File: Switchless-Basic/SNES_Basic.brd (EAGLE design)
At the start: 44.1 x 33 mm, 40 parts

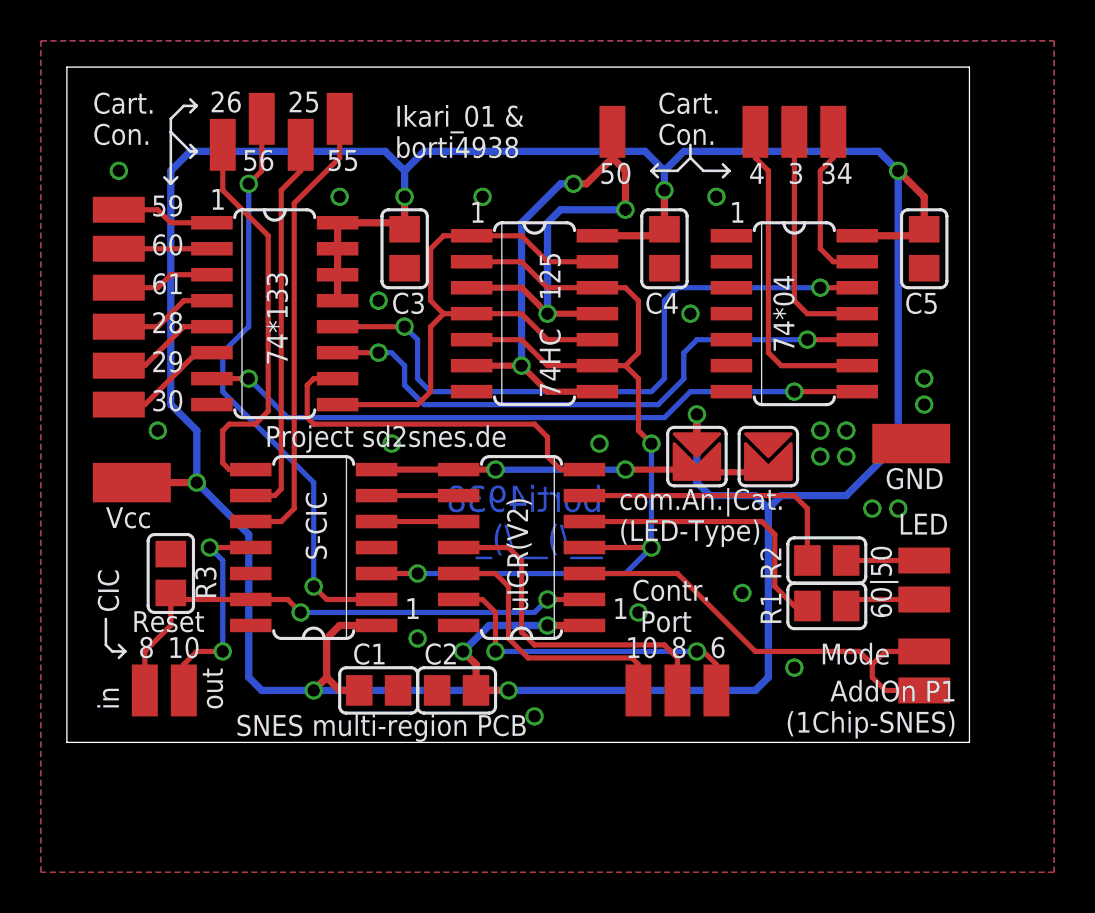
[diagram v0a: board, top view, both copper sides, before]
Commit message: correct two silkscreen errors
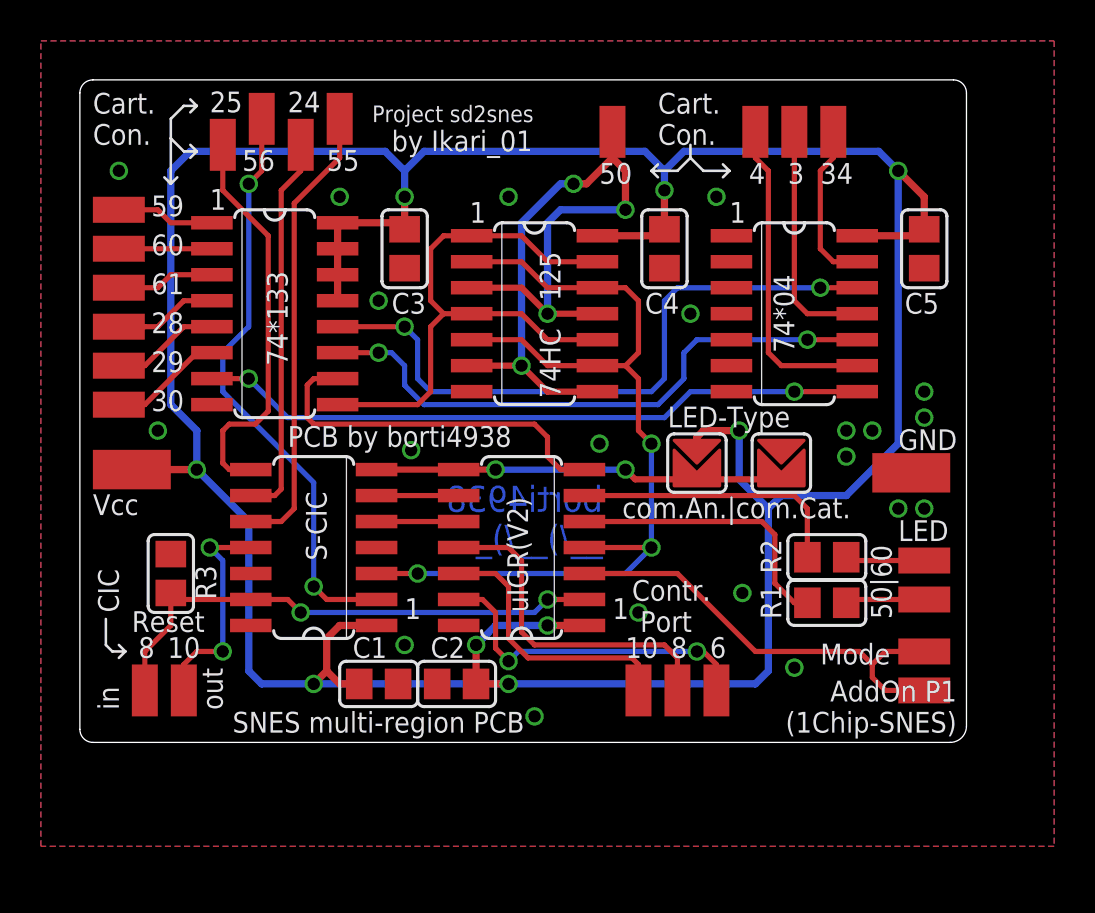
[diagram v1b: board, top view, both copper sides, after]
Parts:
- moved PAD_GND 1.43 mm to (42.5, 19.5)
- moved U$5 0.71 mm to (36.2, 20.0)
- moved PAD_VCC 0.63 mm to (4.45, 19.7)
- moved C1 0.32 mm to (20.3, 9.21)
- moved C2 0.32 mm to (16.5, 9.21)
- moved U$4 0.32 mm to (32.1, 20.0)
- moved R2 0.16 mm to (38.4, 13.2)
- moved R3 0.16 mm to (38.4, 15.4)
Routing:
- net VCC: track 172.4 -> 169.2 mm
- net N$53: track 19.2 -> 20.0 mm
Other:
- board size 44.1 x 33 mm -> 43.3 x 32.4 mm
- board text added: "24"
- board text added: "50|60"
- board text added: "LED-Type"
- board text added: "PCB by borti4938"
- board text added: "Project sd2snes"
- board text added: "by Ikari_01"
- board text added: "com.An.|com.Cat."
- board text removed: "26"
- board text removed: "60|50"
- board text removed: "Ikari_01 & borti4938"
- board text removed: "Project sd2snes.de"
- board text removed: "com.An.|Cat. (LED-Type)"

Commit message: Update DRC to meet OSH Park instead of Itead
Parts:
- moved LED_PAL 9.45 mm to (34.9, 8.73), turned to 180 degrees
- moved LED_NTSC 9.09 mm to (36.8, 8.73), turned to 0 degrees
- moved MODE 4.45 mm to (43.2, 13.3)
- moved MODE1 4.45 mm to (43.2, 15.2)
- moved R2 3.67 mm to (34.8, 13.5), turned to 270 degrees
- moved CPP4 3.18 mm to (29.8, 8.89)
- moved CPP3 3.18 mm to (26.0, 8.89)
- moved CPP2 3.17 mm to (27.9, 8.89)
- moved R3 2.38 mm to (37.0, 13.5), turned to 270 degrees
- moved U$4 2.06 mm to (34.1, 20.0)
- moved U$5 1.27 mm to (37.5, 20.0)
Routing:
- net VCC: track 169.2 -> 164.1 mm
- net N$12: track 13.9 -> 10.6 mm
- net N$46: track 16.6 -> 13.4 mm
- net N$34: track 13.4 -> 10.2 mm
- net N$33: track 16.6 -> 13.4 mm
- net N$53: track 20.0 -> 22.1 mm
- net N$56: track 22.2 -> 21.2 mm, vias 0 -> 2
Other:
- board text added: "(2x)"
- board text added: "Rev.:3.1"
- board text added: "com.An.|Cat."
- board text added: "sd2snes.de by Ikari_01"
- board text removed: "AddOn P1 (1Chip-SNES)"
- board text removed: "Project sd2snes"
- board text removed: "by Ikari_01"
- board text removed: "com.An.|com.Cat."
